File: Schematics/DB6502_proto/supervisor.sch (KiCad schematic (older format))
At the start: 33 parts, among them J4 AVR ISP, J5 Debug UART, J6 USB_B, U12 74AC74, U13 ATmega644PA-PU, U14 74HC595, U15 74HC157, U16 FT230XS, U4 74AC04, U6 74HC74, U7 74AC08, Y1 20MHz

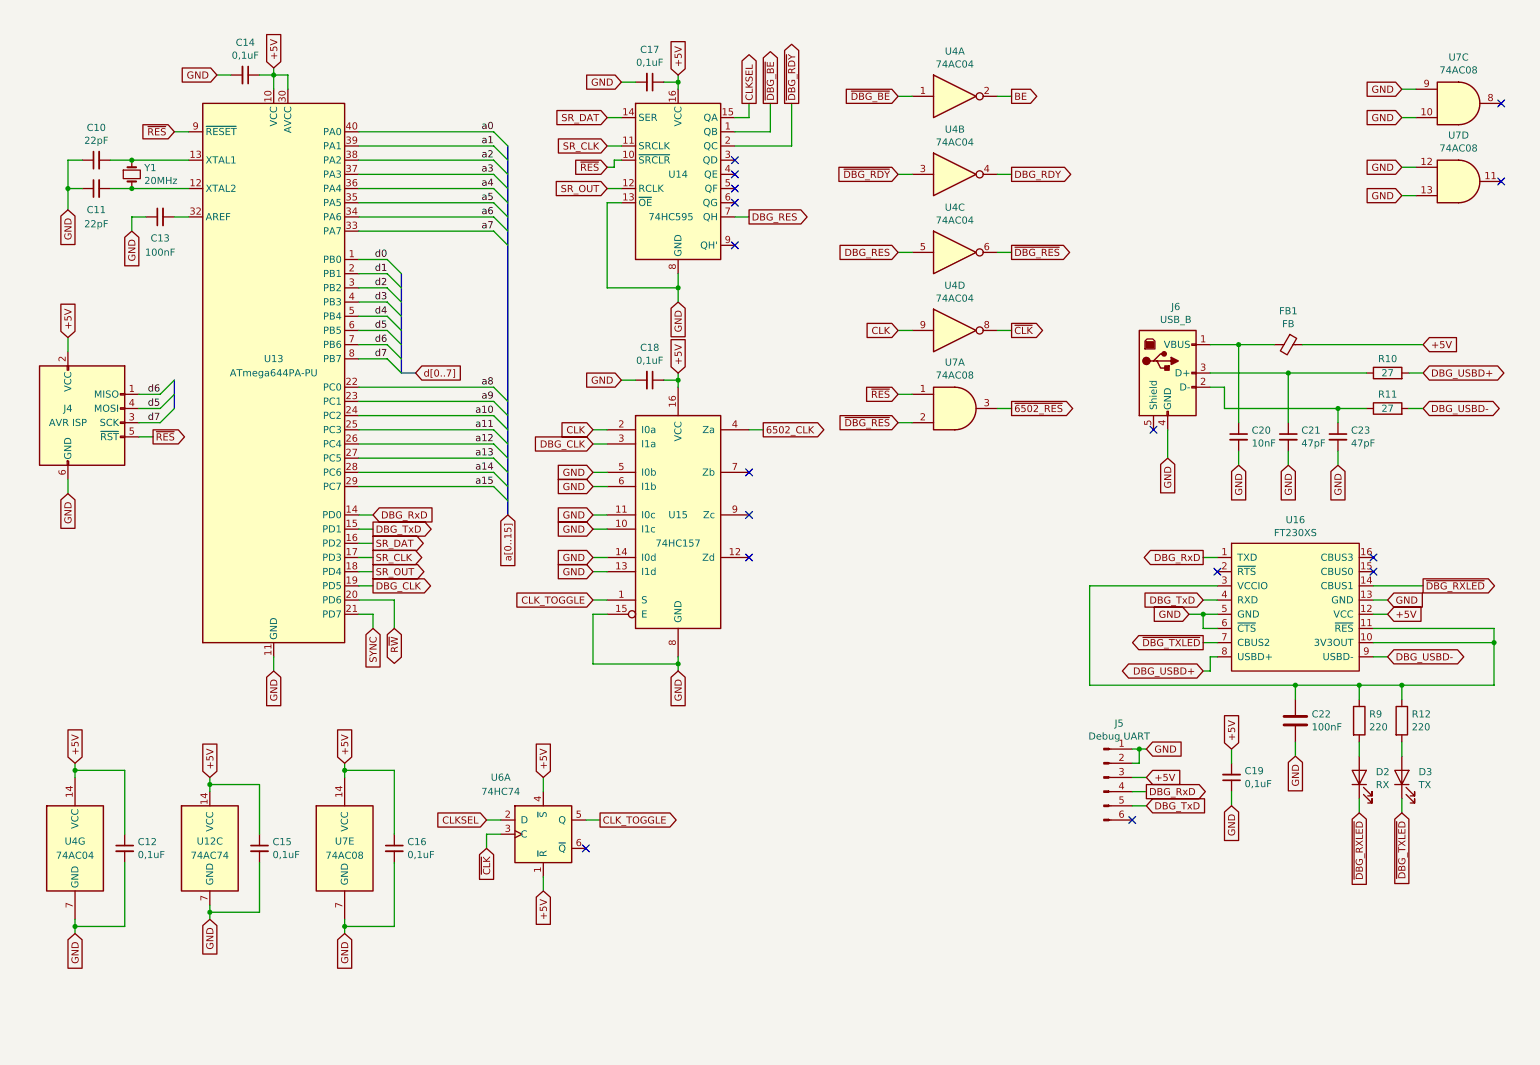
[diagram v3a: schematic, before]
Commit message: Fixed issue with UART CEN during low clock, added IRQ gate
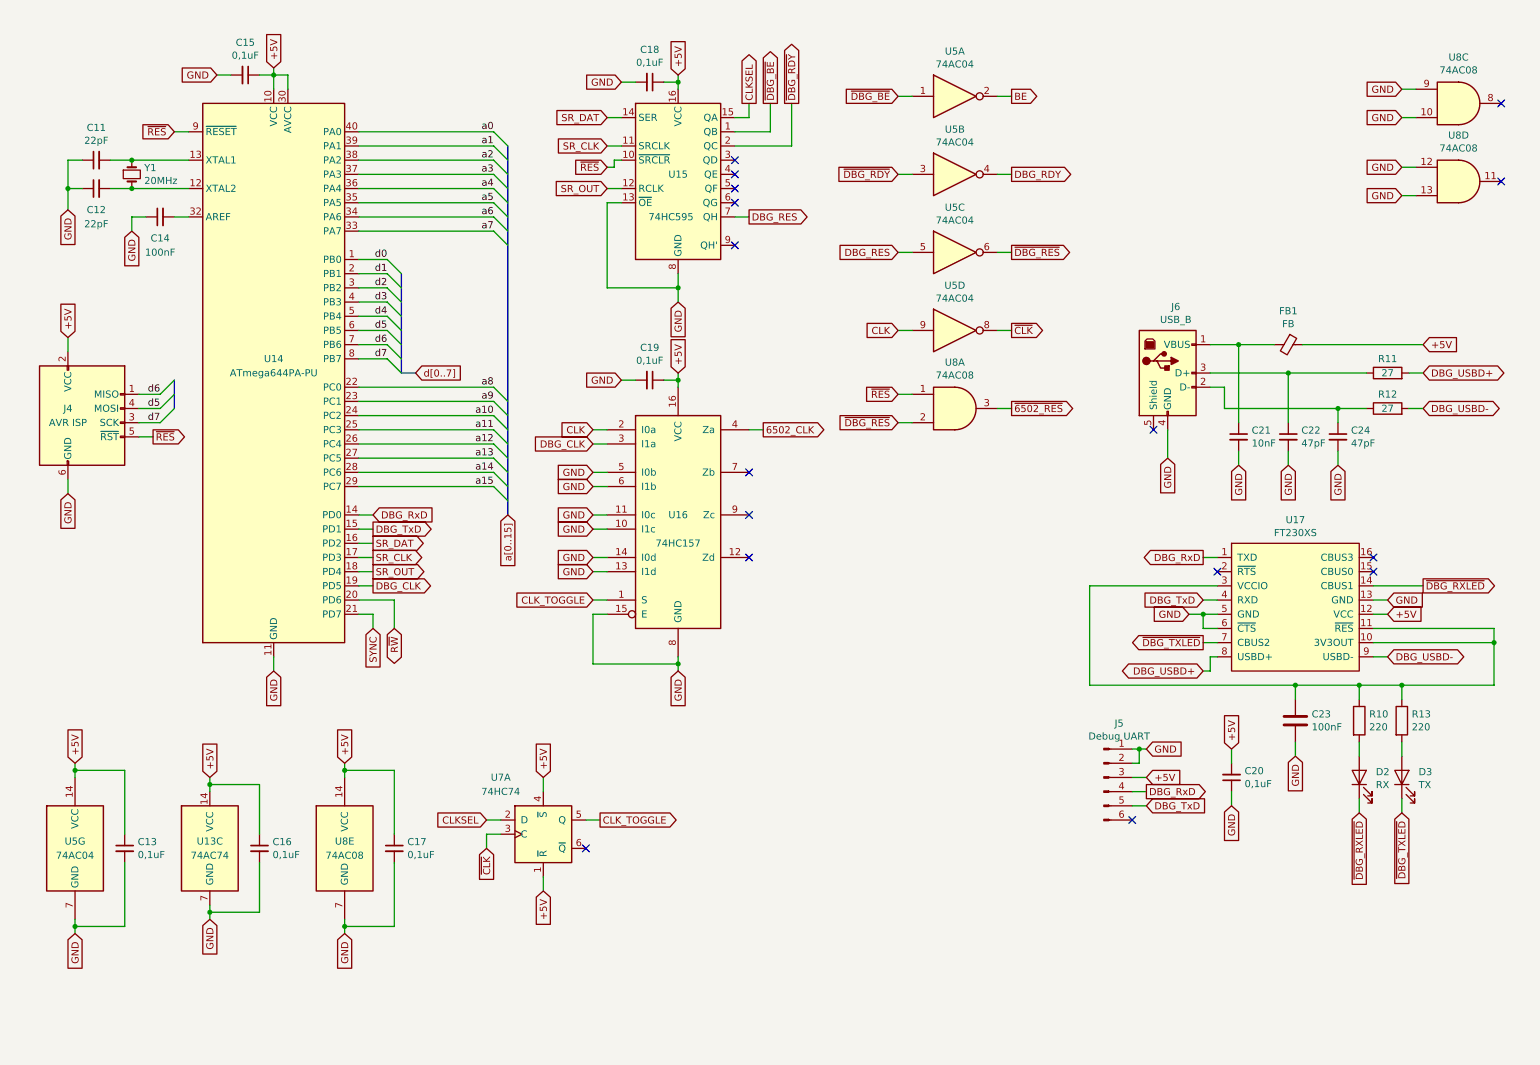
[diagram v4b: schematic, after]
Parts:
- renumbered C10 to C11, C11 to C12, C12 to C13, C13 to C14, C14 to C15, C15 to C16, C16 to C17, C17 to C18, C18 to C19, C19 to C20, C20 to C21, C21 to C22, C22 to C23, C23 to C24, R9 to R10, R10 to R11, R11 to R12, R12 to R13, U12 to U13, U13 to U14, U14 to U15, U15 to U16, U16 to U17, U4 to U5, U6 to U7, U7 to U8
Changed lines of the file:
@@
 $EndComp
 $Comp
-L Device:C_Small C10
+L Device:C_Small C11
 U 1 1 5F942B94
 P 1050 1400
-F 0 "C10" V 1279 1400 50  0000 C CNN
+F 0 "C11" V 1279 1400 50  0000 C CNN
 F 1 "22pF" V 1188 1400 50  0000 C CNN
 F 2 "Capacitor_THT:C_Disc_D5.0mm_W2.5mm_P2.50mm" H 1050 1400 50  0001 C CNN
@@
 $EndComp
 $Comp
-L Device:C_Small C11
+L Device:C_Small C12
 U 1 1 5F942B9A
 P 1050 1600
-F 0 "C11" V 900 1600 50  0000 C CNN
+F 0 "C12" V 900 1600 50  0000 C CNN
 F 1 "22pF" V 800 1600 50  0000 C CNN
 F 2 "Capacitor_THT:C_Disc_D5.0mm_W2.5mm_P2.50mm" H 1050 1600 50  0001 C CNN
@@
 Connection ~ 1300 1600
 $Comp
-L Device:C_Small C13
+L Device:C_Small C14
 U 1 1 5F942BA9
 P 1500 1800
-F 0 "C13" V 1350 1800 50  0000 C CNN
+F 0 "C14" V 1350 1800 50  0000 C CNN
 F 1 "100nF" V 1250 1800 50  0000 C CNN
 F 2 "Capacitor_THT:C_Disc_D5.0mm_W2.5mm_P2.50mm" H 1500 1800 50  0001 C CNN
@@
 	850  1600 850  1750
 $Comp
-L MCU_Microchip_ATmega:ATmega644PA-PU U13
+L MCU_Microchip_ATmega:ATmega644PA-PU U14
 U 1 1 5F942C1A
 P 2300 2900
-F 0 "U13" H 2300 3000 50  0000 C CNN
+F 0 "U14" H 2300 3000 50  0000 C CNN
 F 1 "ATmega644PA-PU" H 2300 2900 50  0000 C CNN
 F 2 "Package_DIP:DIP-40_W15.24mm_Socket" H 2300 2900 50  0001 C CIN
@@
 P 9500 4550
 AR Path="/6014B4D9/5F9AD1D3" Ref="U?"  Part="1"
-AR Path="/5F8F4E1E/5F9AD1D3" Ref="U16"  Part="1"
-F 0 "U16" H 9500 5165 50  0000 C CNN
+AR Path="/5F8F4E1E/5F9AD1D3" Ref="U17"  Part="1"
+F 0 "U17" H 9500 5165 50  0000 C CNN
 F 1 "FT230XS" H 9500 5074 50  0000 C CNN
 F 2 "Package_SO:SSOP-16_5.3x6.2mm_P0.65mm" H 9500 5050 50  0001 C CNN
@@
 P 9500 5350
 AR Path="/6014B4D9/5F9AD1F3" Ref="C?"  Part="1"
-AR Path="/5F8F4E1E/5F9AD1F3" Ref="C22"  Part="1"
-F 0 "C22" H 9615 5396 50  0000 L CNN
+AR Path="/5F8F4E1E/5F9AD1F3" Ref="C23"  Part="1"
+F 0 "C23" H 9615 5396 50  0000 L CNN
 F 1 "100nF" H 9615 5305 50  0000 L CNN
 F 2 "Capacitor_THT:C_Disc_D5.0mm_W2.5mm_P2.50mm" H 9538 5200 50  0001 C CNN
@@
 P 9950 5350
 AR Path="/6014B4D9/5F9AD207" Ref="R?"  Part="1"
-AR Path="/5F8F4E1E/5F9AD207" Ref="R9"  Part="1"
-F 0 "R9" H 10020 5396 50  0000 L CNN
+AR Path="/5F8F4E1E/5F9AD207" Ref="R10"  Part="1"
+F 0 "R10" H 10020 5396 50  0000 L CNN
 F 1 "220" H 10020 5305 50  0000 L CNN
 F 2 "Resistor_THT:R_Axial_DIN0207_L6.3mm_D2.5mm_P10.16mm_Horizontal" V 9880 5350 50  0001 C CNN
@@
 P 10250 5350
 AR Path="/6014B4D9/5F9AD20D" Ref="R?"  Part="1"
-AR Path="/5F8F4E1E/5F9AD20D" Ref="R12"  Part="1"
-F 0 "R12" H 10320 5396 50  0000 L CNN
+AR Path="/5F8F4E1E/5F9AD20D" Ref="R13"  Part="1"
+F 0 "R13" H 10320 5396 50  0000 L CNN
 F 1 "220" H 10320 5305 50  0000 L CNN
 F 2 "Resistor_THT:R_Axial_DIN0207_L6.3mm_D2.5mm_P10.16mm_Horizontal" V 10180 5350 50  0001 C CNN
@@
 P 10150 3150
 AR Path="/6014B4D9/5F9AD22D" Ref="R?"  Part="1"
-AR Path="/5F8F4E1E/5F9AD22D" Ref="R11"  Part="1"
-F 0 "R11" V 10250 3150 50  0000 C CNN
+AR Path="/5F8F4E1E/5F9AD22D" Ref="R12"  Part="1"
+F 0 "R12" V 10250 3150 50  0000 C CNN
 F 1 "27" V 10150 3150 50  0000 C CNN
 F 2 "Resistor_THT:R_Axial_DIN0207_L6.3mm_D2.5mm_P10.16mm_Horizontal" V 10080 3150 50  0001 C CNN
@@
 P 10150 2900
 AR Path="/6014B4D9/5F9AD233" Ref="R?"  Part="1"
-AR Path="/5F8F4E1E/5F9AD233" Ref="R10"  Part="1"
-F 0 "R10" V 10250 2900 50  0000 C CNN
+AR Path="/5F8F4E1E/5F9AD233" Ref="R11"  Part="1"
+F 0 "R11" V 10250 2900 50  0000 C CNN
 F 1 "27" V 10150 2900 50  0000 C CNN
 F 2 "Resistor_THT:R_Axial_DIN0207_L6.3mm_D2.5mm_P10.16mm_Horizontal" V 10080 2900 50  0001 C CNN
@@
 P 9450 3350
 AR Path="/6014B4D9/5F9AD23C" Ref="C?"  Part="1"
-AR Path="/5F8F4E1E/5F9AD23C" Ref="C21"  Part="1"
-F 0 "C21" H 9542 3396 50  0000 L CNN
+AR Path="/5F8F4E1E/5F9AD23C" Ref="C22"  Part="1"
+F 0 "C22" H 9542 3396 50  0000 L CNN
 F 1 "47pF" H 9542 3305 50  0000 L CNN
 F 2 "Capacitor_THT:C_Disc_D5.0mm_W2.5mm_P2.50mm" H 9450 3350 50  0001 C CNN
@@
 P 9800 3350
 AR Path="/6014B4D9/5F9AD242" Ref="C?"  Part="1"
-AR Path="/5F8F4E1E/5F9AD242" Ref="C23"  Part="1"
-F 0 "C23" H 9892 3396 50  0000 L CNN
+AR Path="/5F8F4E1E/5F9AD242" Ref="C24"  Part="1"
+F 0 "C24" H 9892 3396 50  0000 L CNN
 F 1 "47pF" H 9892 3305 50  0000 L CNN
 F 2 "Capacitor_THT:C_Disc_D5.0mm_W2.5mm_P2.50mm" H 9800 3350 50  0001 C CNN
@@
 P 9100 3350
 AR Path="/6014B4D9/5F9AD254" Ref="C?"  Part="1"
-AR Path="/5F8F4E1E/5F9AD254" Ref="C20"  Part="1"
-F 0 "C20" H 9192 3396 50  0000 L CNN
+AR Path="/5F8F4E1E/5F9AD254" Ref="C21"  Part="1"
+F 0 "C21" H 9192 3396 50  0000 L CNN
 F 1 "10nF" H 9192 3305 50  0000 L CNN
 F 2 "Capacitor_THT:C_Disc_D5.0mm_W2.5mm_P2.50mm" H 9100 3350 50  0001 C CNN
@@
 	8450 5950 8350 5950
 $Comp
-L 74xx:74HC595 U14
+L 74xx:74HC595 U15
 U 1 1 5F9C2188
 P 5150 1500
-F 0 "U14" H 5150 1500 50  0000 C CNN
+F 0 "U15" H 5150 1500 50  0000 C CNN
 F 1 "74HC595" H 5100 1200 50  0000 C CNN
 F 2 "" H 5150 1500 50  0001 C CNN
@@
 NoConn ~ 5550 2000
 $Comp
-L 74xx:74LS04 U4
+L 74xx:74LS04 U5
 U 1 1 5F92D3FA
 P 7100 950
-F 0 "U4" H 7100 1267 50  0000 C CNN
+F 0 "U5" H 7100 1267 50  0000 C CNN
 F 1 "74AC04" H 7100 1176 50  0000 C CNN
 F 2 "" H 7100 950 50  0001 C CNN
@@
 	7400 950  7500 950
 $Comp
-L 74xx:74LS04 U4
+L 74xx:74LS04 U5
 U 2 1 5F93AD6D
 P 7100 1500
-F 0 "U4" H 7100 1817 50  0000 C CNN
+F 0 "U5" H 7100 1817 50  0000 C CNN
 F 1 "74AC04" H 7100 1726 50  0000 C CNN
 F 2 "" H 7100 1500 50  0001 C CNN
@@
 	7400 1500 7500 1500
 $Comp
-L 74xx:74LS04 U4
+L 74xx:74LS04 U5
 U 7 1 5F946300
 P 900 6250
-F 0 "U4" H 900 6300 50  0000 C CNN
+F 0 "U5" H 900 6300 50  0000 C CNN
 F 1 "74AC04" H 900 6200 50  0000 C CNN
 F 2 "" H 900 6250 50  0001 C CNN
@@
 	900  5650 900  5700
 $Comp
-L 74xx:74LS04 U4
+L 74xx:74LS04 U5
 U 3 1 5F95A89B
 P 7100 2050
-F 0 "U4" H 7100 2367 50  0000 C CNN
+F 0 "U5" H 7100 2367 50  0000 C CNN
 F 1 "74AC04" H 7100 2276 50  0000 C CNN
 F 2 "" H 7100 2050 50  0001 C CNN
@@
 $EndComp
 $Comp
-L 74xx:74LS04 U4
+L 74xx:74LS04 U5
 U 4 1 5F95B175
 P 7100 2600
-F 0 "U4" H 7100 2917 50  0000 C CNN
+F 0 "U5" H 7100 2917 50  0000 C CNN
 F 1 "74AC04" H 7100 2826 50  0000 C CNN
 F 2 "" H 7100 2600 50  0001 C CNN
@@
 	7400 2050 7500 2050
 $Comp
-L 74xx:74LS08 U7
+L 74xx:74LS08 U8
 U 1 1 5F991189
 P 7100 3150
-F 0 "U7" H 7100 3475 50  0000 C CNN
+F 0 "U8" H 7100 3475 50  0000 C CNN
 F 1 "74AC08" H 7100 3384 50  0000 C CNN
 F 2 "" H 7100 3150 50  0001 C CNN
@@
 	7500 3150 7400 3150
 $Comp
-L 74xx:74LS157 U15
+L 74xx:74LS157 U16
 U 1 1 5F9A90DC
 P 5150 3900
-F 0 "U15" H 5150 3900 50  0000 C CNN
+F 0 "U16" H 5150 3900 50  0000 C CNN
 F 1 "74HC157" H 5150 3700 50  0000 C CNN
 F 2 "" H 5150 3900 50  0001 C CNN
@@
 	7400 2600 7500 2600
 $Comp
-L 74xx:74HC74 U12
+L 74xx:74HC74 U13
 U 3 1 5FA1E8BB
 P 1850 6250
-F 0 "U12" H 1850 6300 50  0000 C CNN
+F 0 "U13" H 1850 6300 50  0000 C CNN
 F 1 "74AC74" H 1850 6200 50  0000 C CNN
 F 2 "" H 1850 6250 50  0001 C CNN
@@
 	1850 5750 1850 5800
 $Comp
-L 74xx:74HC74 U6
+L 74xx:74HC74 U7
 U 1 1 5FA3C995
 P 4200 6150
-F 0 "U6" H 3900 6550 50  0000 C CNN
+F 0 "U7" H 3900 6550 50  0000 C CNN
 F 1 "74HC74" H 3900 6450 50  0000 C CNN
 F 2 "" H 4200 6150 50  0001 C CNN
@@
 	4550 4500 4650 4500
 $Comp
-L Device:C_Small C12
+L Device:C_Small C13
 U 1 1 5FAB56CF
 P 1250 6250
-F 0 "C12" H 1342 6296 50  0000 L CNN
+F 0 "C13" H 1342 6296 50  0000 L CNN
 F 1 "0,1uF" H 1342 6205 50  0000 L CNN
 F 2 "" H 1250 6250 50  0001 C CNN
@@
 $EndComp
 $Comp
-L Device:C_Small C15
+L Device:C_Small C16
 U 1 1 5FAB6000
 P 2200 6250
-F 0 "C15" H 2292 6296 50  0000 L CNN
+F 0 "C16" H 2292 6296 50  0000 L CNN
 F 1 "0,1uF" H 2292 6205 50  0000 L CNN
 F 2 "" H 2200 6250 50  0001 C CNN
@@
 	1850 5800 1850 5850
 $Comp
-L Device:C_Small C18
+L Device:C_Small C19
 U 1 1 5FAF8D14
 P 4950 2950
-F 0 "C18" V 4721 2950 50  0000 C CNN
+F 0 "C19" V 4721 2950 50  0000 C CNN
 F 1 "0,1uF" V 4812 2950 50  0000 C CNN
 F 2 "" H 4950 2950 50  0001 C CNN
@@
 	5150 2950 5150 3000
 $Comp
-L 74xx:74LS08 U7
+L 74xx:74LS08 U8
 U 5 1 5FB0D0DC
 P 2800 6250
-F 0 "U7" H 2800 6300 50  0000 C CNN
+F 0 "U8" H 2800 6300 50  0000 C CNN
 F 1 "74AC08" H 2800 6200 50  0000 C CNN
 F 2 "" H 2800 6250 50  0001 C CNN
@@
 GND
 $Comp
-L Device:C_Small C16
+L Device:C_Small C17
 U 1 1 5FB0F869
 P 3150 6250
-F 0 "C16" H 3242 6296 50  0000 L CNN
+F 0 "C17" H 3242 6296 50  0000 L CNN
 F 1 "0,1uF" H 3242 6205 50  0000 L CNN
 F 2 "" H 3150 6250 50  0001 C CNN
@@
 	2800 6800 2800 6850
 $Comp
-L Device:C_Small C14
+L Device:C_Small C15
 U 1 1 5FB3967F
 P 2100 800
-F 0 "C14" V 1871 800 50  0000 C CNN
+F 0 "C15" V 1871 800 50  0000 C CNN
 F 1 "0,1uF" V 1962 800 50  0000 C CNN
 F 2 "" H 2100 800 50  0001 C CNN
@@
 	2200 800  2300 800
 $Comp
-L Device:C_Small C17
+L Device:C_Small C18
 U 1 1 5FB5019A
 P 4950 850
-F 0 "C17" V 4721 850 50  0000 C CNN
+F 0 "C18" V 4721 850 50  0000 C CNN
 F 1 "0,1uF" V 4812 850 50  0000 C CNN
 F 2 "" H 4950 850 50  0001 C CNN
@@
 	5150 850  5150 900
 $Comp
-L 74xx:74LS08 U7
+L 74xx:74LS08 U8
 U 3 1 5FBB3E3E
 P 10650 1000
-F 0 "U7" H 10650 1325 50  0000 C CNN
+F 0 "U8" H 10650 1325 50  0000 C CNN
 F 1 "74AC08" H 10650 1234 50  0000 C CNN
 F 2 "" H 10650 1000 50  0001 C CNN
@@
 NoConn ~ 10950 1000
 $Comp
-L Device:C_Small C19
+L Device:C_Small C20
 U 1 1 5FC939BD
 P 9050 5750
-F 0 "C19" H 8958 5704 50  0000 R CNN
+F 0 "C20" H 8958 5704 50  0000 R CNN
 F 1 "0,1uF" H 8958 5795 50  0000 R CNN
 F 2 "" H 9050 5750 50  0001 C CNN
@@
 GND
 $Comp
-L 74xx:74LS08 U7
+L 74xx:74LS08 U8
 U 4 1 5FBB5F74
 P 10650 1550
-F 0 "U7" H 10650 1875 50  0000 C CNN
+F 0 "U8" H 10650 1875 50  0000 C CNN
 F 1 "74AC08" H 10650 1784 50  0000 C CNN
 F 2 "" H 10650 1550 50  0001 C CNN
